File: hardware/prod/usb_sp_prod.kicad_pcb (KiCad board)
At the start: 4 copper layers, 38.1 x 53.9 mm, 49 parts, among them U1 CH32V203C8U6, U10 SN74LVC1G32DBVR, U2 ZD24C02B-MAGMT, U3 32.768kHz, U4 KH-TYPE-C-16P, U5 SD101CWS, U6 CH572D, U9 SN74LVC1G32DBVR, X1 8MHz, X2 XTM20032000DT00351001

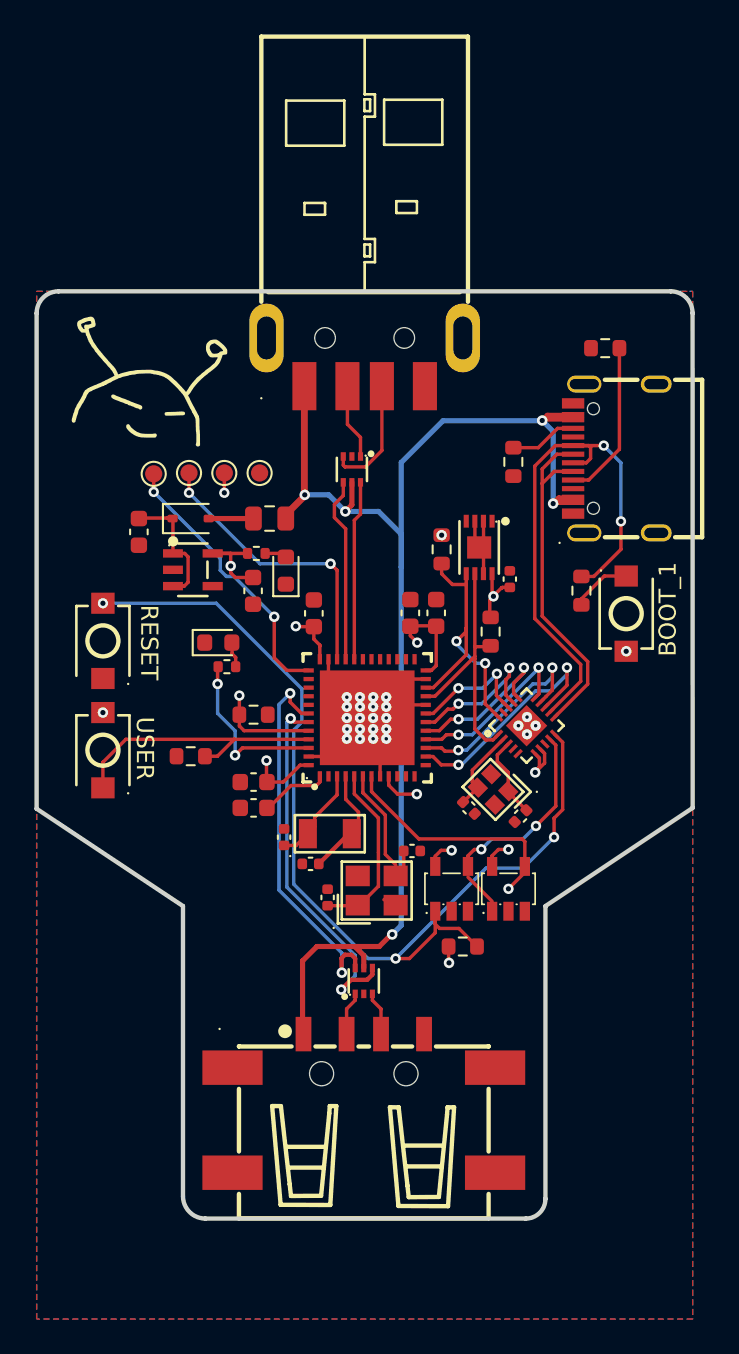
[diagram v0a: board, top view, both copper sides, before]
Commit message: feat(hardware-prod): replace mode transistors with TPS2121 power mux
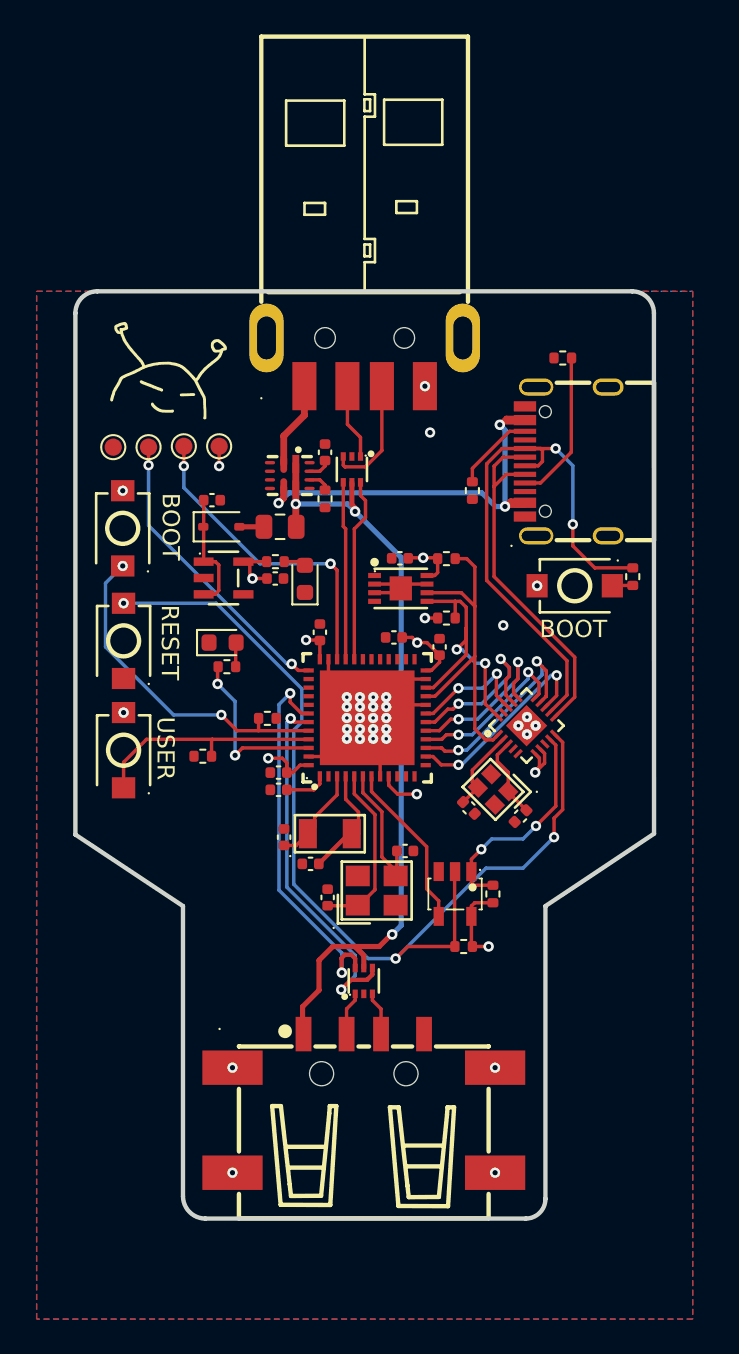
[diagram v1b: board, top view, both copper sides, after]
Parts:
- removed U10, U9: SN74LVC1G32DBVR, usb_sp_fp:SOT-23-5_L3.0-W1.7-P0.95-LS2.8-BR
- added C15: 100nF, Capacitor_SMD:C_0402_1005Metric, F.Cu at (143.6, 76.1)
- added R13: 10kΩ, Resistor_SMD:R_0402_1005Metric, F.Cu at (153.3, 101.8)
- added R14: 25.5kΩ, Resistor_SMD:R_0402_1005Metric, F.Cu at (143.6, 78.8)
- added RESET2: ~, usb_sp_fp:SW-SMD_L3.9-W3.0-P4.45, F.Cu at (131.8, 80.5)
- added U7: SN74LVC1G08DBVR, usb_sp_fp:SOT-23-5_L3.0-W1.7-P0.95-LS2.8-BR, F.Cu at (151.1, 101.8)
- added U8: TPS2121RUXR, usb_sp_fp:VQFN-HR-12_L2.5-W2.0-P0.50-BL, F.Cu at (141.5, 77.5)
- C1, C13, C2, C6, C7, C8, C9: footprint Capacitor_SMD:C_0603_1608Metric -> Capacitor_SMD:C_0402_1005Metric
- R1, R10, R2, R3, R4, R5, R6, R9: footprint Resistor_SMD:R_0603_1608Metric -> Resistor_SMD:R_0402_1005Metric
- moved TP4 8.63 mm to (131.3, 75.8)
- moved C5 6.49 mm to (147.9, 82.3), turned to 180 degrees
- moved U2 5.14 mm to (148.0, 84.0), turned to -90 degrees
- moved R10 4.95 mm to (150.6, 82.3), turned to 0 degrees
- moved C1 4.63 mm to (137.0, 78.9), turned to 180 degrees
- moved R9 4.00 mm to (150.6, 85.7), turned to 0 degrees
- moved BOOT_1 3.40 mm to (158.1, 83.9), turned to 0 degrees
- moved R1 3.09 mm to (161.4, 83.3)
- moved R3 2.90 mm to (152.1, 78.3)
- moved U4 2.80 mm to (157.6, 76.6)
- moved R2 2.53 mm to (157.4, 70.6)
- moved C8 1.98 mm to (150.2, 87.4)
- moved LDO1 1.85 mm to (137.7, 83.4)
- moved U5 1.85 mm to (137.6, 80.4)
- moved C13 1.79 mm to (140.9, 95.7)
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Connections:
- R4 pad 2: +3V3 -> /CH32V203/BOOT_0
- U1 pad 44: +3V3 -> /CH32V203/BOOT_0
- U4 pad A4: VBUS -> USB_2_VBUS
- U4 pad A9: VBUS -> USB_2_VBUS
- U4 pad B4: VBUS -> USB_2_VBUS
- U4 pad B9: VBUS -> USB_2_VBUS
- USB1 pad 1: VBUS -> USB_1_VBUS
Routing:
- net VBUS: track 78.3 -> 45.7 mm, vias 5 -> 3
- net USB_2_VBUS: track 0.00 -> 25.2 mm, vias 0 -> 3
- net /CH32V203/BOOT_0: track 0.00 -> 19.6 mm, vias 0 -> 2
- net +3V3: track 39.2 -> 27.8 mm, vias 15 -> 13
- net USB_1_VBUS: track 0.00 -> 5.01 mm
- net /CH32V203/RST_CH32: track 14.1 -> 9.68 mm, vias 1 -> 0
- net /CH32V203/EEPROM_SCL: track 15.5 -> 19.4 mm
- net Net-(BOOT_1-Pad2): track 3.50 -> 1.17 mm
- net /CH32V203/PB10: track 16.0 -> 13.7 mm
- net /CH32V203/SPI_CS: track 13.8 -> 12.1 mm
- net /CH32V203/SWDIO: track 16.9 -> 18.5 mm
- net Net-(U1-VBAT): track 3.88 -> 2.44 mm
- net Net-(U8-ILM): track 0.00 -> 1.31 mm
- net /CH32V203/GPIO_I2C_CTRL: track 8.92 -> 10.2 mm
- net Net-(U8-SS): track 0.00 -> 1.24 mm
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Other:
- board size 38.1 x 53.9 mm -> 33.6 x 53.9 mm
- board text added: "BOOT"
